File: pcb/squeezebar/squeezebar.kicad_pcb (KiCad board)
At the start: 2 copper layers, 73.7 x 20.3 mm, 41 parts

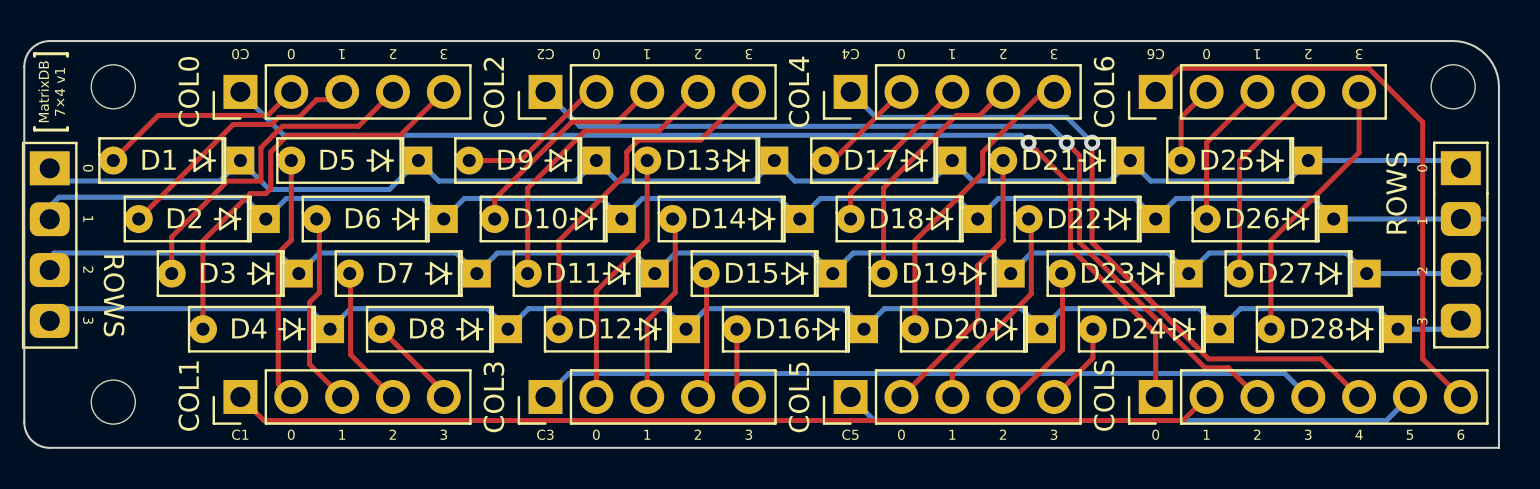
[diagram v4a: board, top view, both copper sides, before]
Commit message: Add numbers for mounting holes
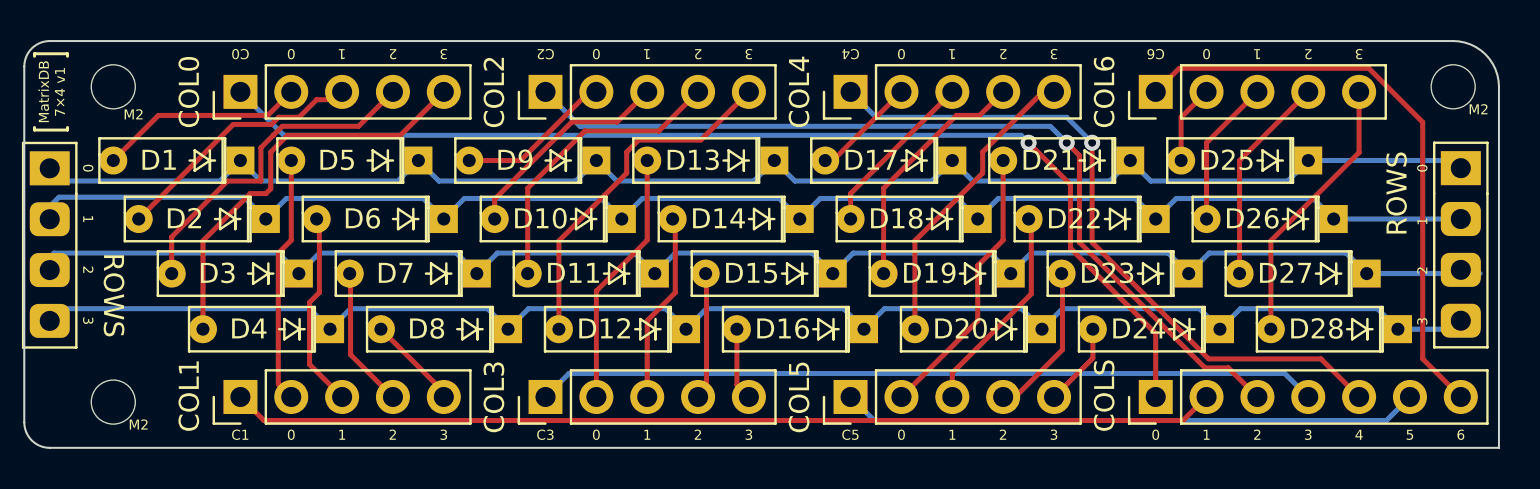
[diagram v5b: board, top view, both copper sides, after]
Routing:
- net /c4: track 41.9 -> 34.6 mm
- net /r1: track 78.3 -> 77.1 mm
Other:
- board text added: "M2"
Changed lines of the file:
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@@
       (layer "B.Paste" (type "Bottom Solder Paste"))
       (layer "B.SilkS" (type "Bottom Silk Screen"))
+      (copper_finish "None")
       (dielectric_constraints no)
     )
@@
   (gr_line (start 48.895 77.47) (end 61.595 77.47) (layer "B.SilkS") (width 0.15))
   (gr_line (start 79.375 62.865) (end 79.375 59.69) (layer "B.SilkS") (width 0.15))
-  (gr_line (start 33.02 77.47) (end 46.355 77.47) (layer "B.SilkS") (width 0.15))
+  (gr_line (start 33.655 77.47) (end 46.99 77.47) (layer "B.SilkS") (width 0.15))
   (gr_line (start 27.305 64.135) (end 27.305 73.025) (layer "B.SilkS") (width 0.15))
   (gr_line (start 95.25 64.135) (end 95.25 73.025) (layer "B.SilkS") (width 0.15))
@@
     (effects (font (size 0.5 0.5) (thickness 0.125)))
   )
+  (gr_text "M2" (at 30.226 62.103) (layer "F.SilkS")
+    (effects (font (size 0.5 0.5) (thickness 0.125)))
+  )
   (gr_text "3" (at 45.72 59.055 180) (layer "F.SilkS")
     (effects (font (size 0.5 0.5) (thickness 0.125)))
@@
     (effects (font (size 0.5 0.5) (thickness 0.125)))
   )
+  (gr_text "M2" (at 30.48 77.597) (layer "F.SilkS")
+    (effects (font (size 0.5 0.5) (thickness 0.125)))
+  )
   (gr_text "1" (at 40.64 78.105) (layer "F.SilkS")
     (effects (font (size 0.5 0.5) (thickness 0.125)))
@@
   )
   (gr_text "C2" (at 50.8 59.055 180) (layer "F.SilkS")
+    (effects (font (size 0.5 0.5) (thickness 0.125)))
+  )
+  (gr_text "M2" (at 97.409 61.849) (layer "F.SilkS")
     (effects (font (size 0.5 0.5) (thickness 0.125)))
   )
@@
     (effects (font (size 0.5 0.5) (thickness 0.125)))
   )
+  (dimension (type aligned) (layer "B.SilkS")
+    (pts (xy 29.21 78.74) (xy 29.21 76.454))
+    (height -1.397)
+    (gr_text "2.3 mm" (at 27.305 77.597 90) (layer "B.SilkS")
+      (effects (font (size 0.3 0.3) (thickness 0.1)) (justify mirror))
+    )
+    (format (units 3) (units_format 1) (precision 1))
+    (style (thickness 0.1) (arrow_length 0.3) (text_position_mode 2) (extension_height 0.58642) (extension_offset 0) keep_text_aligned)
+  )
+  (dimension (type aligned) (layer "B.SilkS")
+    (pts (xy 24.765 76.454) (xy 29.21 76.454))
+    (height -1.397)
+    (gr_text "4.45 mm" (at 27.051 74.676) (layer "B.SilkS")
+      (effects (font (size 0.3 0.3) (thickness 0.1)) (justify mirror))
+    )
+    (format (units 3) (units_format 1) (precision 2))
+    (style (thickness 0.1) (arrow_length 0.3) (text_position_mode 2) (extension_height 0.58642) (extension_offset 0) keep_text_aligned)
+  )
   (dimension (type aligned) (layer "Dwgs.User")
-    (pts (xy 24.765 58.42) (xy 99.187 58.293))
+    (pts (xy 24.765 58.42) (xy 98.425 58.42))
     (height -3.81)
-    (gr_text "74.4221 mm" (at 61.967536 53.396508 0.09777427286) (layer "Dwgs.User")
+    (gr_text "73.6600 mm" (at 61.595 53.46) (layer "Dwgs.User")
       (effects (font (size 1 1) (thickness 0.15)))
     )
@@
   (segment (start 63.254511 65.413511) (end 62.23 64.389) (width 0.25) (layer "B.Cu") (net 1))
   (segment (start 34.535489 65.413511) (end 26.033511 65.413511) (width 0.25) (layer "B.Cu") (net 1))
+  (segment (start 43.425489 65.413511) (end 44.45 64.389) (width 0.25) (layer "B.Cu") (net 1))
   (segment (start 71.12 64.389) (end 70.095489 65.413511) (width 0.25) (layer "B.Cu") (net 1))
   (segment (start 62.23 64.389) (end 61.205489 65.413511) (width 0.25) (layer "B.Cu") (net 1))
   (segment (start 80.01 64.389) (end 78.985489 65.413511) (width 0.25) (layer "B.Cu") (net 1))
-  (segment (start 44.45 64.389) (end 43.003031 65.835969) (width 0.25) (layer "B.Cu") (net 1))
   (segment (start 87.875489 65.413511) (end 81.034511 65.413511) (width 0.25) (layer "B.Cu") (net 1))
   (segment (start 44.45 64.389) (end 45.474511 65.413511) (width 0.25) (layer "B.Cu") (net 1))
   (segment (start 35.56 64.389) (end 34.535489 65.413511) (width 0.25) (layer "B.Cu") (net 1))
-  (segment (start 43.003031 65.835969) (end 37.006969 65.835969) (width 0.25) (layer "B.Cu") (net 1))
+  (segment (start 35.56 64.389) (end 36.584511 65.413511) (width 0.25) (layer "B.Cu") (net 1))
   (segment (start 81.034511 65.413511) (end 80.01 64.389) (width 0.25) (layer "B.Cu") (net 1))
+  (segment (start 43.425489 65.413511) (end 36.584511 65.413511) (width 0.25) (layer "B.Cu") (net 1))
   (segment (start 78.985489 65.413511) (end 72.144511 65.413511) (width 0.25) (layer "B.Cu") (net 1))
   (segment (start 54.364511 65.413511) (end 53.34 64.389) (width 0.25) (layer "B.Cu") (net 1))
-  (segment (start 37.006969 65.835969) (end 35.56 64.389) (width 0.25) (layer "B.Cu") (net 1))
   (segment (start 61.205489 65.413511) (end 54.364511 65.413511) (width 0.25) (layer "B.Cu") (net 1))
   (segment (start 45.474511 65.413511) (end 52.315489 65.413511) (width 0.25) (layer "B.Cu") (net 1))
@@
   (segment (start 62.475489 66.285489) (end 55.634511 66.285489) (width 0.25) (layer "B.Cu") (net 3))
   (segment (start 53.585489 66.285489) (end 54.61 67.31) (width 0.25) (layer "B.Cu") (net 3))
+  (segment (start 90.17 67.31) (end 96.52 67.31) (width 0.25) (layer "B.Cu") (net 3))
   (segment (start 71.365489 66.285489) (end 64.524511 66.285489) (width 0.25) (layer "B.Cu") (net 3))
   (segment (start 55.634511 66.285489) (end 54.61 67.31) (width 0.25) (layer "B.Cu") (net 3))
@@
   (segment (start 63.5 67.31) (end 62.475489 66.285489) (width 0.25) (layer "B.Cu") (net 3))
   (segment (start 73.414511 66.285489) (end 72.39 67.31) (width 0.25) (layer "B.Cu") (net 3))
-  (segment (start 97.67 67.31) (end 90.17 67.31) (width 0.25) (layer "B.Cu") (net 3))
   (segment (start 35.738878 66.218878) (end 36.83 67.31) (width 0.25) (layer "B.Cu") (net 3))
   (segment (start 25.4 67.32) (end 26.501122 66.218878) (width 0.25) (layer "B.Cu") (net 3))
@@
   (segment (start 51.974511 75.025489) (end 87.725489 75.025489) (width 0.25) (layer "B.Cu") (net 24))
   (segment (start 87.725489 75.025489) (end 88.9 76.2) (width 0.25) (layer "B.Cu") (net 24))
-  (segment (start 83.236001 73.608999) (end 83.922001 74.295) (width 0.25) (layer "F.Cu") (net 25))
   (segment (start 78.105 63.5) (end 78.105 68.477998) (width 0.25) (layer "F.Cu") (net 25))
   (segment (start 89.535 74.295) (end 91.44 76.2) (width 0.25) (layer "F.Cu") (net 25))
-  (segment (start 78.105 68.477999) (end 83.236001 73.608999) (width 0.25) (layer "F.Cu") (net 25))
-  (segment (start 78.105 68.477998) (end 83.236001 73.608999) (width 0.25) (layer "F.Cu") (net 25))
+  (segment (start 78.105 68.477998) (end 83.922001 74.295) (width 0.25) (layer "F.Cu") (net 25))
   (segment (start 83.922001 74.295) (end 89.535 74.295) (width 0.25) (layer "F.Cu") (net 25))
   (via (at 78.105 63.5) (size 0.8) (drill 0.4) (layers "F.Cu" "B.Cu") (net 25))

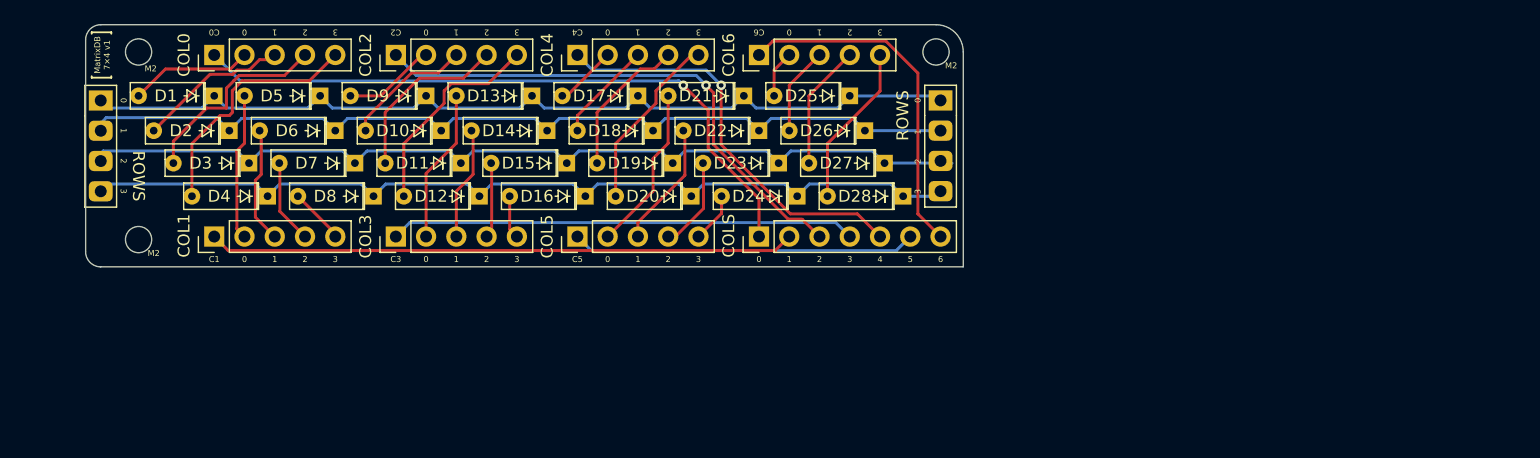
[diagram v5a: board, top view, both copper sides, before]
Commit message: Squeezebar PCB: Add MCU. It's no longer a daughterboard...
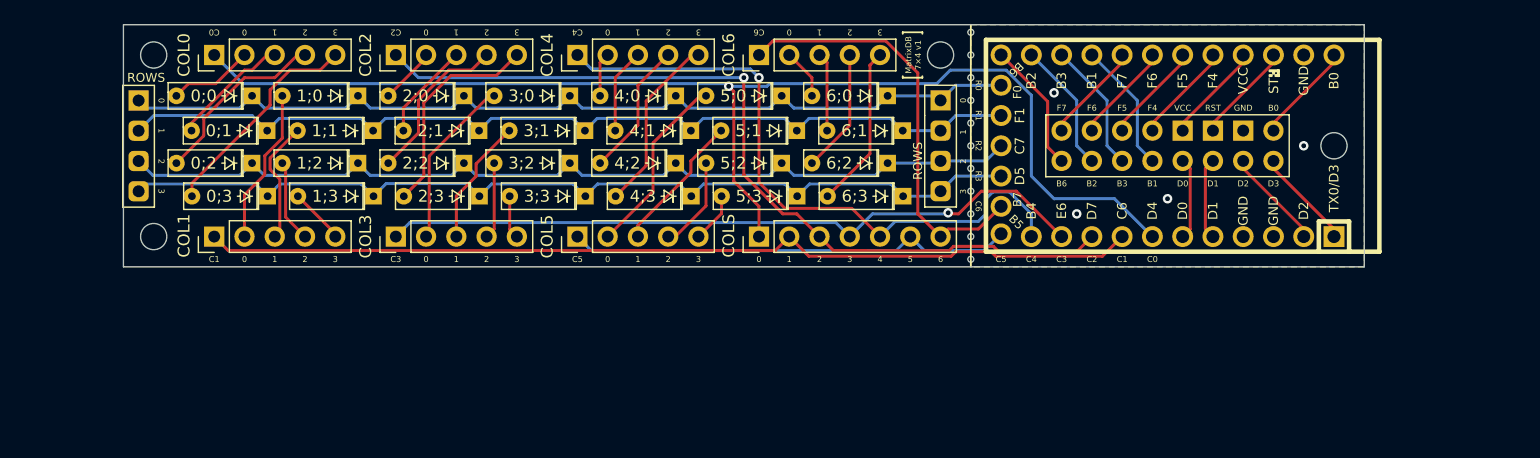
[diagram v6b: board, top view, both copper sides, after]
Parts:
- added H2: MountingHole, MountingHole:MountingHole_2.2mm_M2_DIN965, F.Cu at (129.5, 68.6)
- added J2: Conn_02x08_Counter_Clockwise, Library:PinSocket_2x08_P2.54mm_Bespoke, F.Cu at (124.5, 69.8)
- added REF**: breakaway-hole, Library:breakaway-hole, F.Cu at (99.1, 62.9)
- added REF**: breakaway-hole, Library:breakaway-hole, F.Cu at (99.1, 64.8)
- added REF**: breakaway-hole, Library:breakaway-hole, F.Cu at (99.1, 74.3)
- added REF**: breakaway-hole, Library:breakaway-hole, F.Cu at (99.1, 68.6)
- added REF**: breakaway-hole, Library:breakaway-hole, F.Cu at (99.1, 66.7)
- added REF**: breakaway-hole, Library:breakaway-hole, F.Cu at (99.1, 76.2)
- added REF**: breakaway-hole, Library:breakaway-hole, F.Cu at (99.1, 70.5)
- added REF**: breakaway-hole, Library:breakaway-hole, F.Cu at (99.1, 78.1)
- added REF**: breakaway-hole, Library:breakaway-hole, F.Cu at (99.1, 72.4)
- added REF**: breakaway-hole, Library:breakaway-hole, F.Cu at (99.1, 61.0)
- added REF**: breakaway-hole, Library:breakaway-hole, F.Cu at (99.1, 59.1)
- added U1: Elite-C, 3dmodels:Elite-C, B.Cu at (115.6, 68.6)
- moved 0;1 3.18 mm to (40.0, 67.3)
- moved 1;1 3.18 mm to (48.9, 67.3)
- moved 3;0 3.18 mm to (65.4, 64.4)
- moved ROWS2 3.18 mm to (29.2, 64.8)
- moved 0;0 3.17 mm to (38.7, 64.4)
- moved 1;0 3.17 mm to (47.6, 64.4)
- moved 2;0 3.17 mm to (56.5, 64.4)
- moved 2;1 3.17 mm to (57.8, 67.3)
- moved 3;1 3.17 mm to (66.7, 67.3)
- moved 4;0 3.17 mm to (74.3, 64.4)
- moved 4;1 3.17 mm to (75.6, 67.3)
- moved 5;0 3.17 mm to (83.2, 64.4)
- moved 5;1 3.17 mm to (84.5, 67.3)
- moved 6;0 3.17 mm to (92.1, 64.4)
- moved 6;1 3.17 mm to (93.3, 67.3)
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- renumbered D1 to 0;0, D2 to 0;1, D3 to 0;2, D4 to 0;3, D5 to 1;0, D6 to 1;1, D7 to 1;2, D8 to 1;3, D9 to 2;0, D10 to 2;1, D11 to 2;2, D12 to 2;3, D13 to 3;0, D14 to 3;1, D15 to 3;2, D16 to 3;3, D17 to 4;0, D18 to 4;1, D19 to 4;2, D20 to 4;3, D21 to 5;0, D22 to 5;1, D23 to 5;2, D24 to 5;3, D25 to 6;0, D26 to 6;1, D27 to 6;2, D28 to 6;3
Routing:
- net /c0: track 55.8 -> 103.8 mm
- net /c1: track 49.2 -> 78.9 mm
- net /c2: track 44.4 -> 70.8 mm
- net /c3: track 39.1 -> 60.0 mm, vias 0 -> 1
- net /c4: track 34.6 -> 54.5 mm
- net /pb6: track 0.00 -> 11.0 mm
- net /pb2: track 0.00 -> 11.0 mm
- net /pb3: track 0.00 -> 11.0 mm
- net /pb1: track 0.00 -> 11.0 mm
- net /c5: track 28.9 -> 37.6 mm
- net /vcc: track 0.00 -> 7.18 mm
- net /rst: track 0.00 -> 7.18 mm
- net /pf7: track 0.00 -> 7.18 mm
- net /pf6: track 0.00 -> 7.18 mm
- net /pf5: track 0.00 -> 7.18 mm
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- added copper zone on B.Cu, net /gnd
- added copper zone on F.Cu, net /gnd
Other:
- board size 73.7 x 20.3 mm -> 104.1 x 20.3 mm
- board text added: "B0"
- board text added: "B1"
- board text added: "B2"
- board text added: "B3"
- board text added: "B6"
- board text added: "D0"
- board text added: "D1"
- board text added: "D2"
- board text added: "D3"
- board text added: "F4"
- board text added: "F5"
- board text added: "F6"
- board text added: "F7"
- board text added: "GND"
- board text added: "R0"
- board text added: "R1"
- board text added: "R2"
- board text added: "R3"
- board text added: "RST"
- board text added: "VCC"

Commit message: MatrixBar: Use Pro Micro pins for the rows/cols
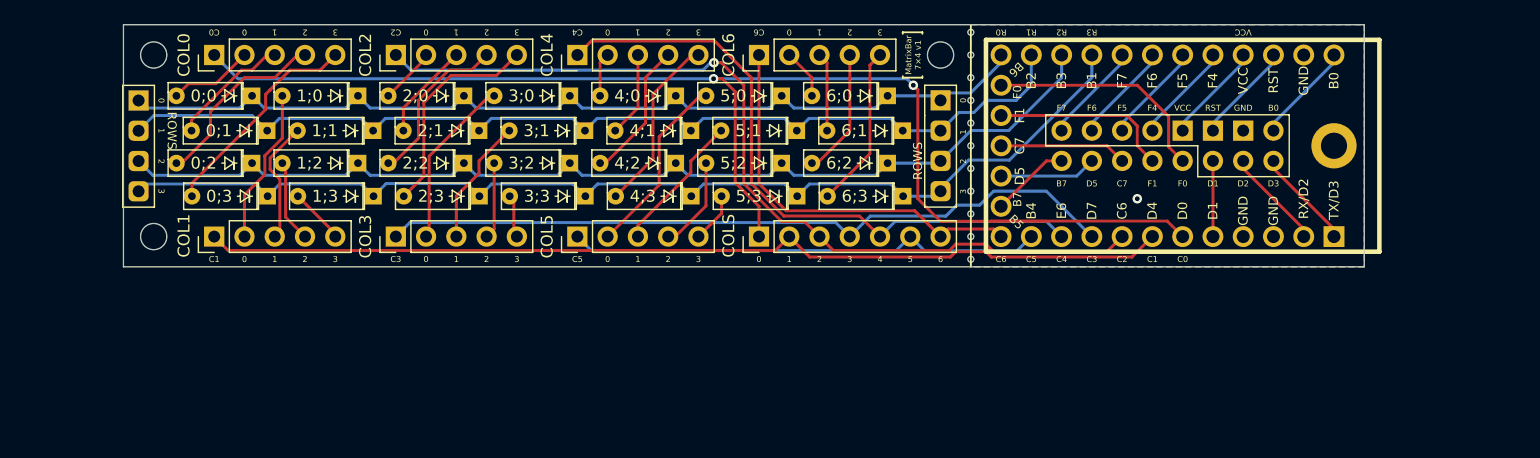
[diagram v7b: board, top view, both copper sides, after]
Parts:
- removed the H2 at (129.5, 68.6)
- added H4: MountingHole, MountingHole:MountingHole_2.2mm_M2_DIN965, F.Cu at (30.5, 76.2)
- H1: footprint MountingHole:MountingHole_2.2mm_M2_DIN965 -> MountingHole:MountingHole_2.2mm_M2_DIN965_Pad
- moved H1 99.4 mm to (129.5, 68.6)
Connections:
- J2 pad 11: /pb3 -> /pc7
- J2 pad 13: /pb2 -> /pd5
- J2 pad 15: /pb6 -> /pb7
- J2 pad 7: /pd0 -> /pf0
- J2 pad 9: /pb1 -> /pf1
- U1 pad 10: /c3 -> /c4
- U1 pad 11: /c4 -> /c5
- U1 pad 12: /c5 -> /c6
- U1 pad 13: /pb6 -> /r0
- U1 pad 14: /pb2 -> /r1
- U1 pad 15: /pb3 -> /r2
- U1 pad 16: /pb1 -> /r3
- U1 pad 25: /c6 -> /pb7
- U1 pad 26: /r3 -> /pd5
- U1 pad 27: /r2 -> /pc7
- U1 pad 28: /r1 -> /pf1
- U1 pad 29: /r0 -> /pf0
- U1 pad 6: /pd0 -> /c0
- U1 pad 7: /c0 -> /c1
- U1 pad 8: /c1 -> /c2
- U1 pad 9: /c2 -> /c3
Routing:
- net /pf0: track 0.00 -> 19.4 mm
- net /pf1: track 0.00 -> 15.3 mm
- net /r3: track 77.4 -> 90.3 mm
- net /pb6: track 11.0 -> 0.00 mm
- net /pb2: track 11.0 -> 0.00 mm
- net /pb3: track 11.0 -> 0.00 mm
- net /pb1: track 11.0 -> 0.00 mm
- net /pc7: track 0.00 -> 10.7 mm
- net /r2: track 78.7 -> 88.1 mm
- net /pd5: track 0.00 -> 8.15 mm
- net /pd0: track 6.88 -> 0.00 mm
- net /pb7: track 0.00 -> 6.66 mm
- net /r1: track 79.1 -> 85.2 mm
- net /c0: track 103.8 -> 108.2 mm, vias 1 -> 2
- net /c2: track 70.8 -> 74.1 mm
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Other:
- board text added: "B7"
- board text added: "C7"
- board text added: "D5"
- board text added: "F0"
- board text added: "F1"
- board text added: "MatrixBar 7×4 v1"
- board text removed: "B1"
- board text removed: "B2"
- board text removed: "B3"
- board text removed: "B6"
- board text removed: "D0"
- board text removed: "MatrixDB 7×4 v1"
